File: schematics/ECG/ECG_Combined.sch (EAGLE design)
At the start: 72 parts, among them IC1 ADS1293, IC2 LIS3DH, IC3 MCP1703, IC4 CC2541, IC5 FSA4157, IC6 FSA4157, IC7 FSA4157, IC8 BALUN_2450BM_SERIES_SMD, X1 XTAL-2SMD, X2 XTAL_403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

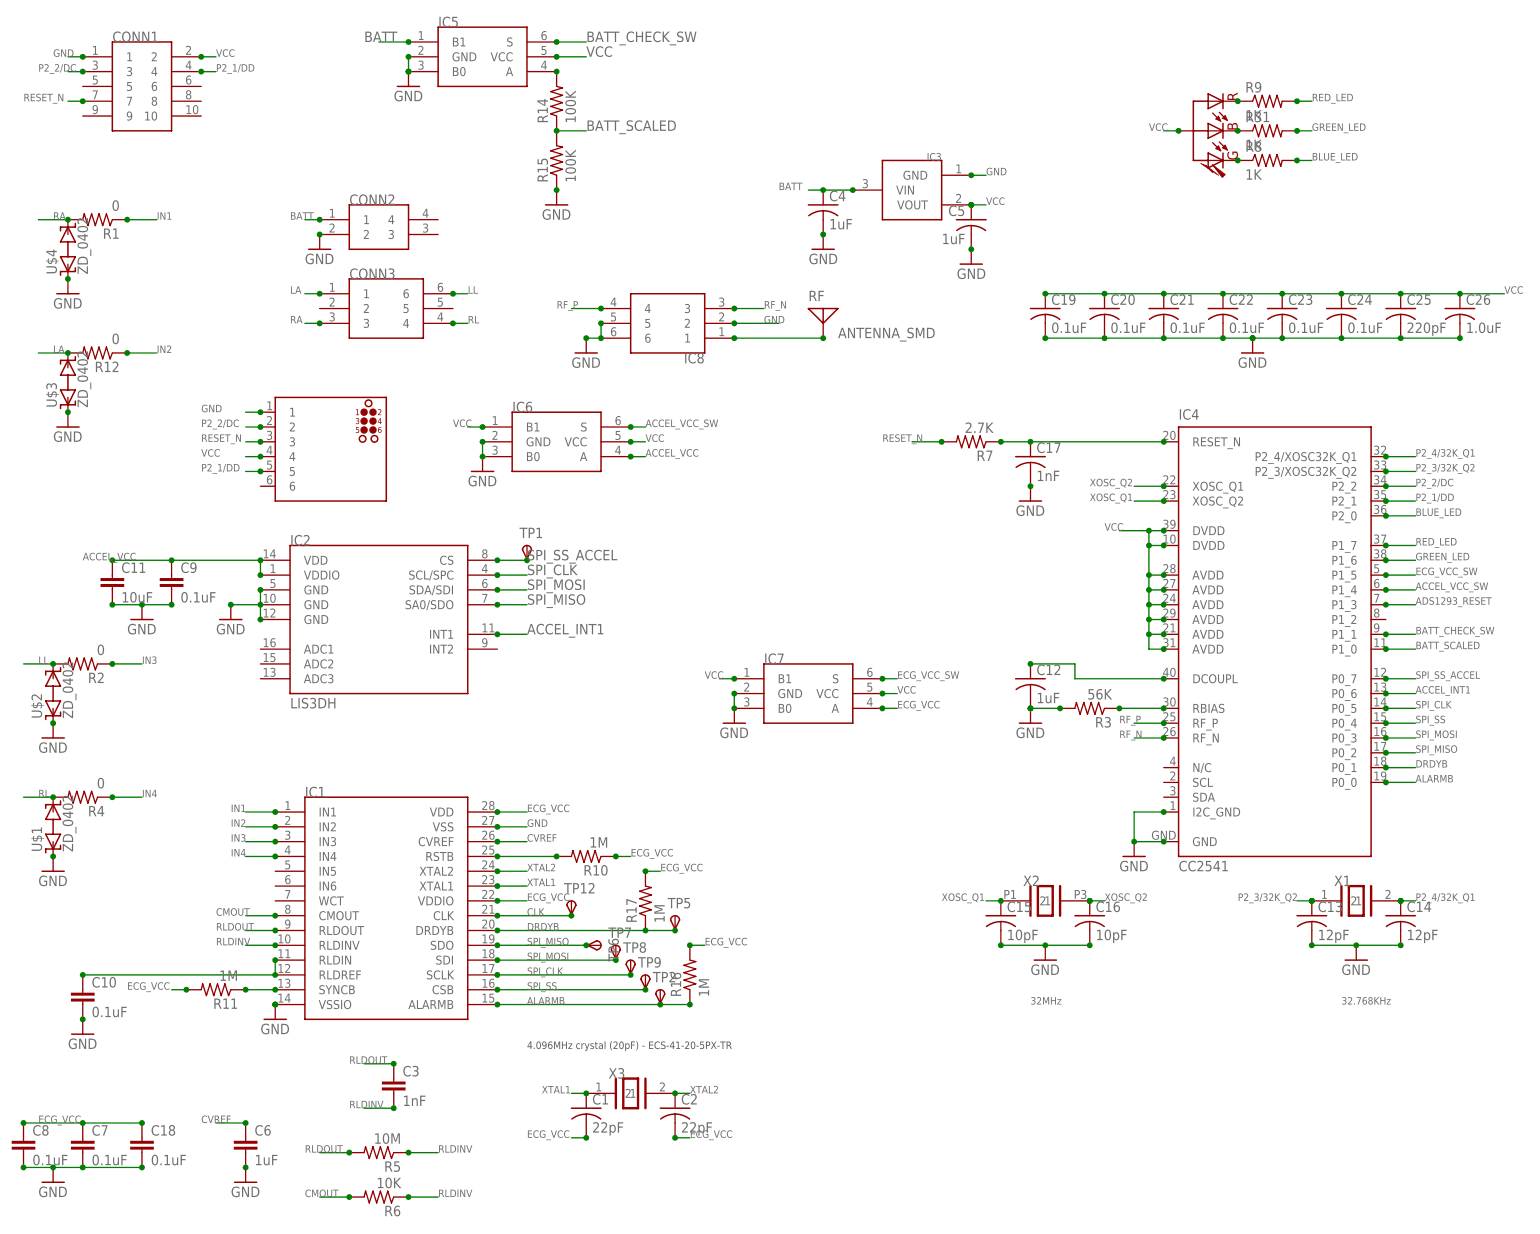
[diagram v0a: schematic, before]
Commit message: added 50ohm antenna trace. renamed TVS components
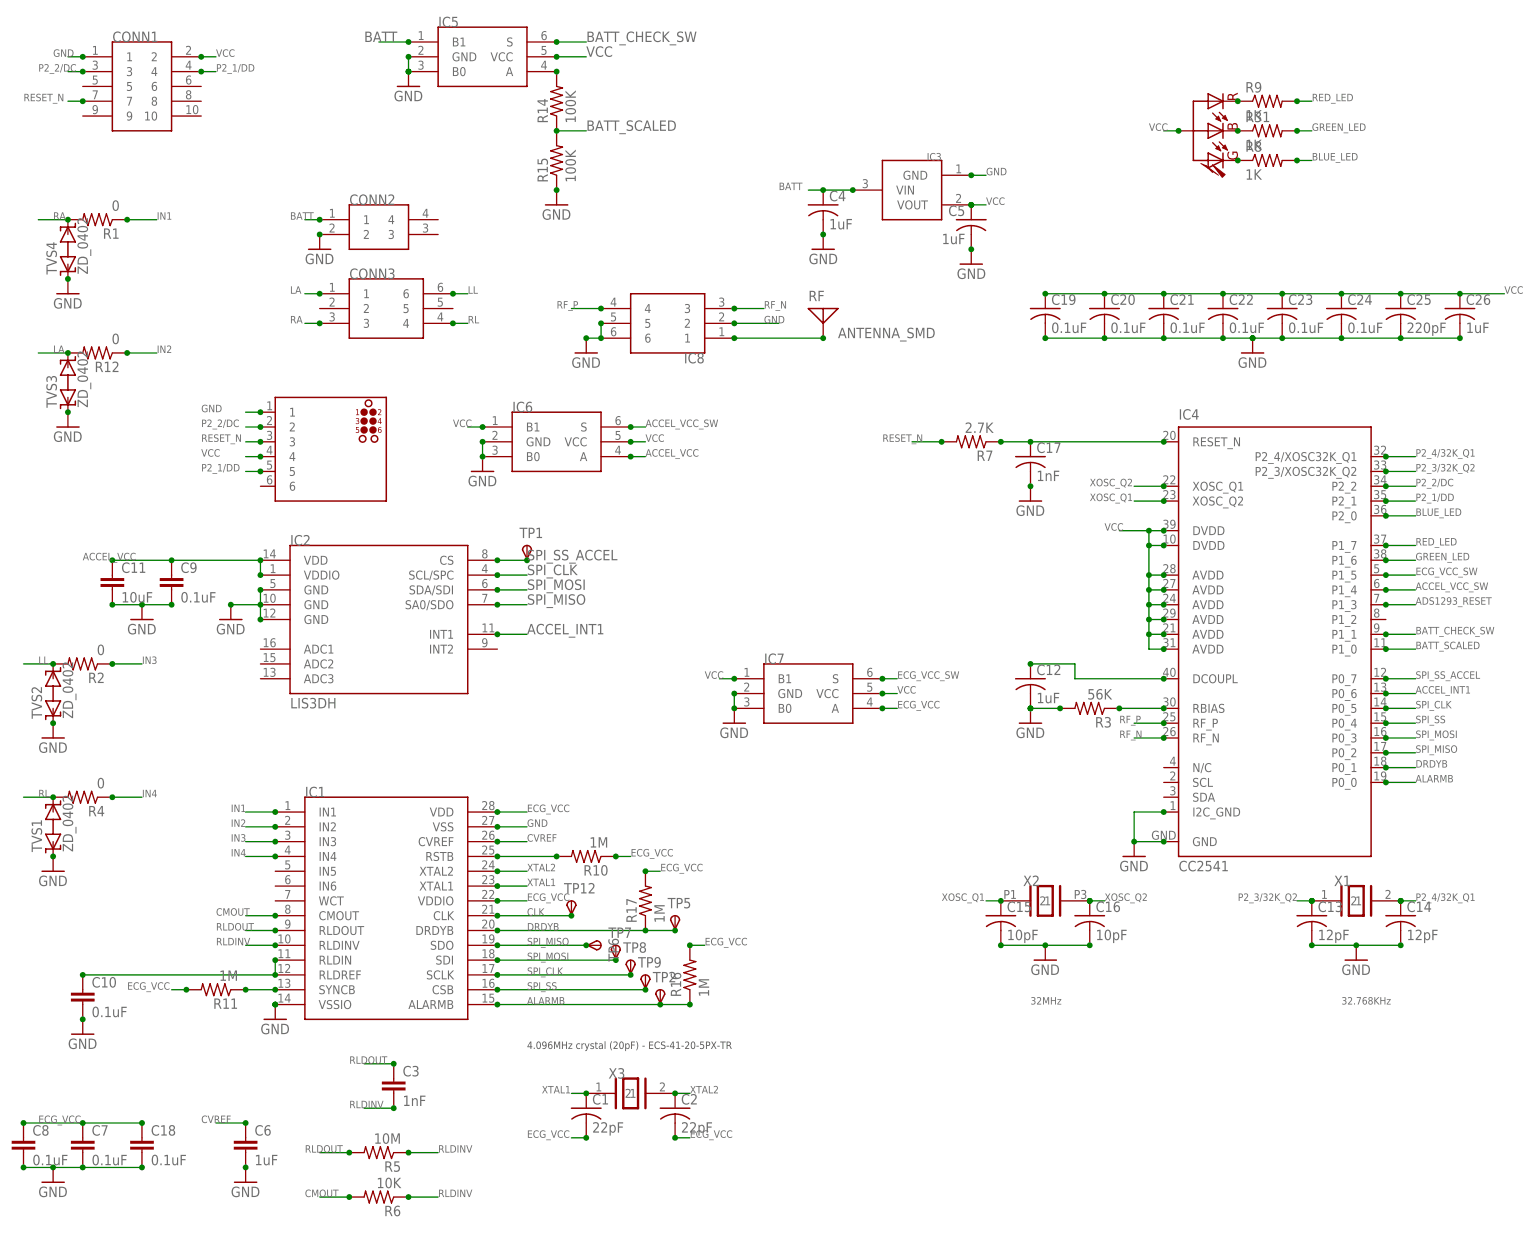
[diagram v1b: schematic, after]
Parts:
- C26: value 1.0uF -> 1uF
- renumbered U$1 to TVS1, U$2 to TVS2, U$3 to TVS3, U$4 to TVS4, U$5 to PROG
